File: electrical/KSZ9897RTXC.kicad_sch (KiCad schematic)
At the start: 1 part, among them U1 KSZ9897RTXC

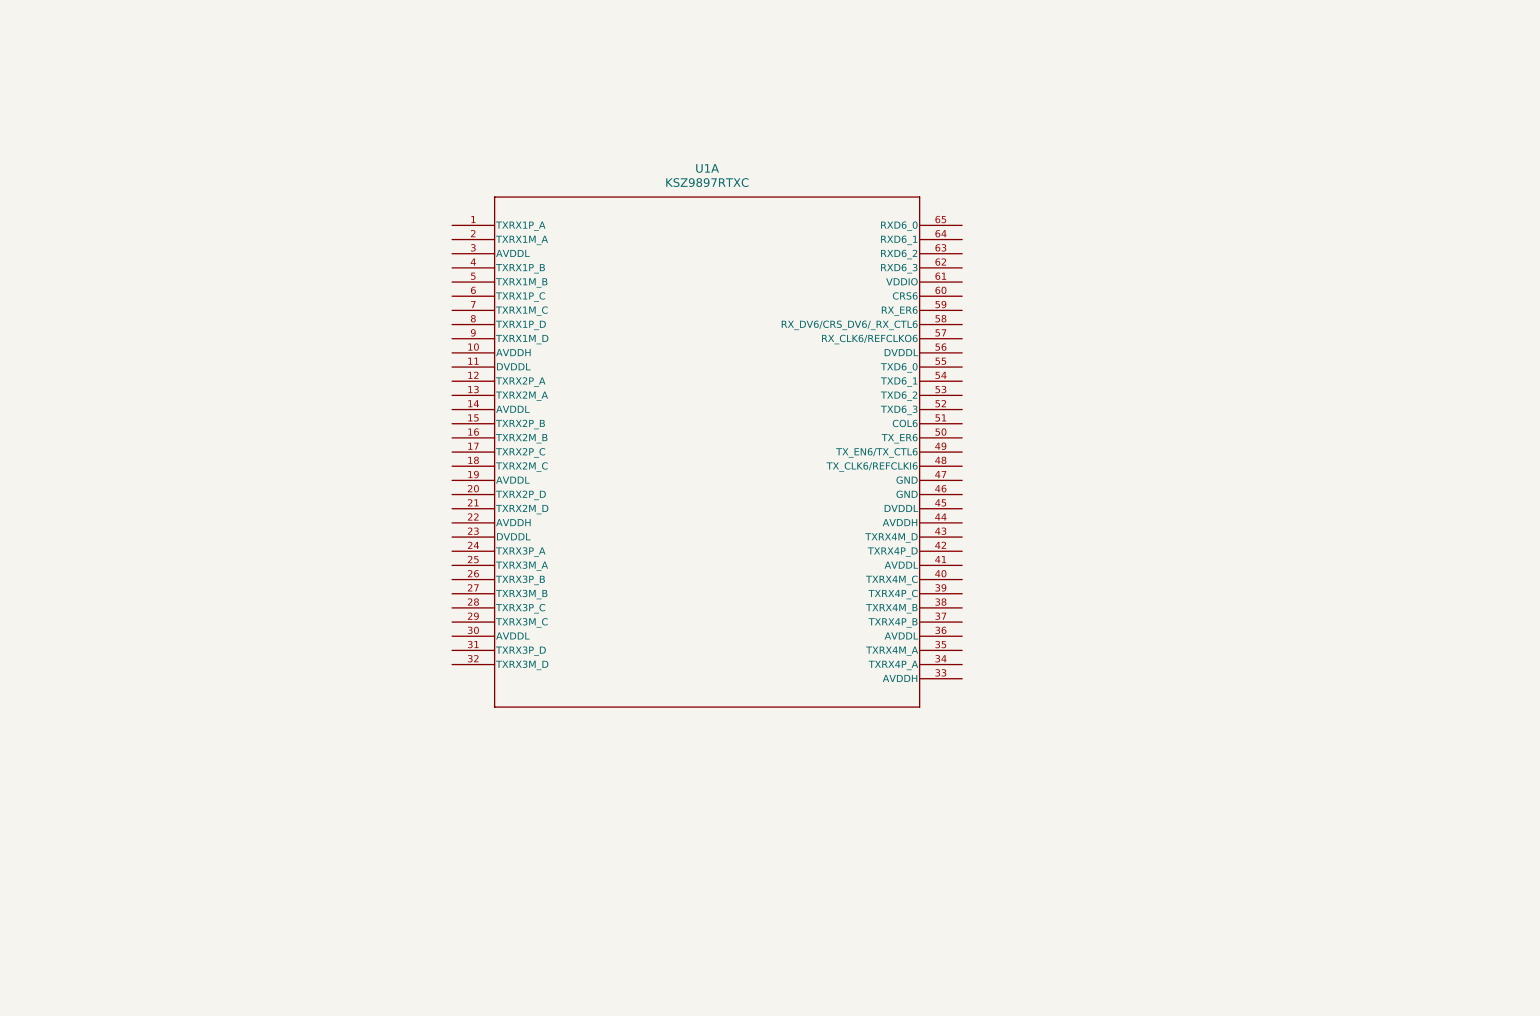
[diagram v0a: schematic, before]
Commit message: RJ-45 <-> KSZ9897R schematic connections
Also switched to a different RJ-45 port: Belfuse 0826-1G1T-23-F
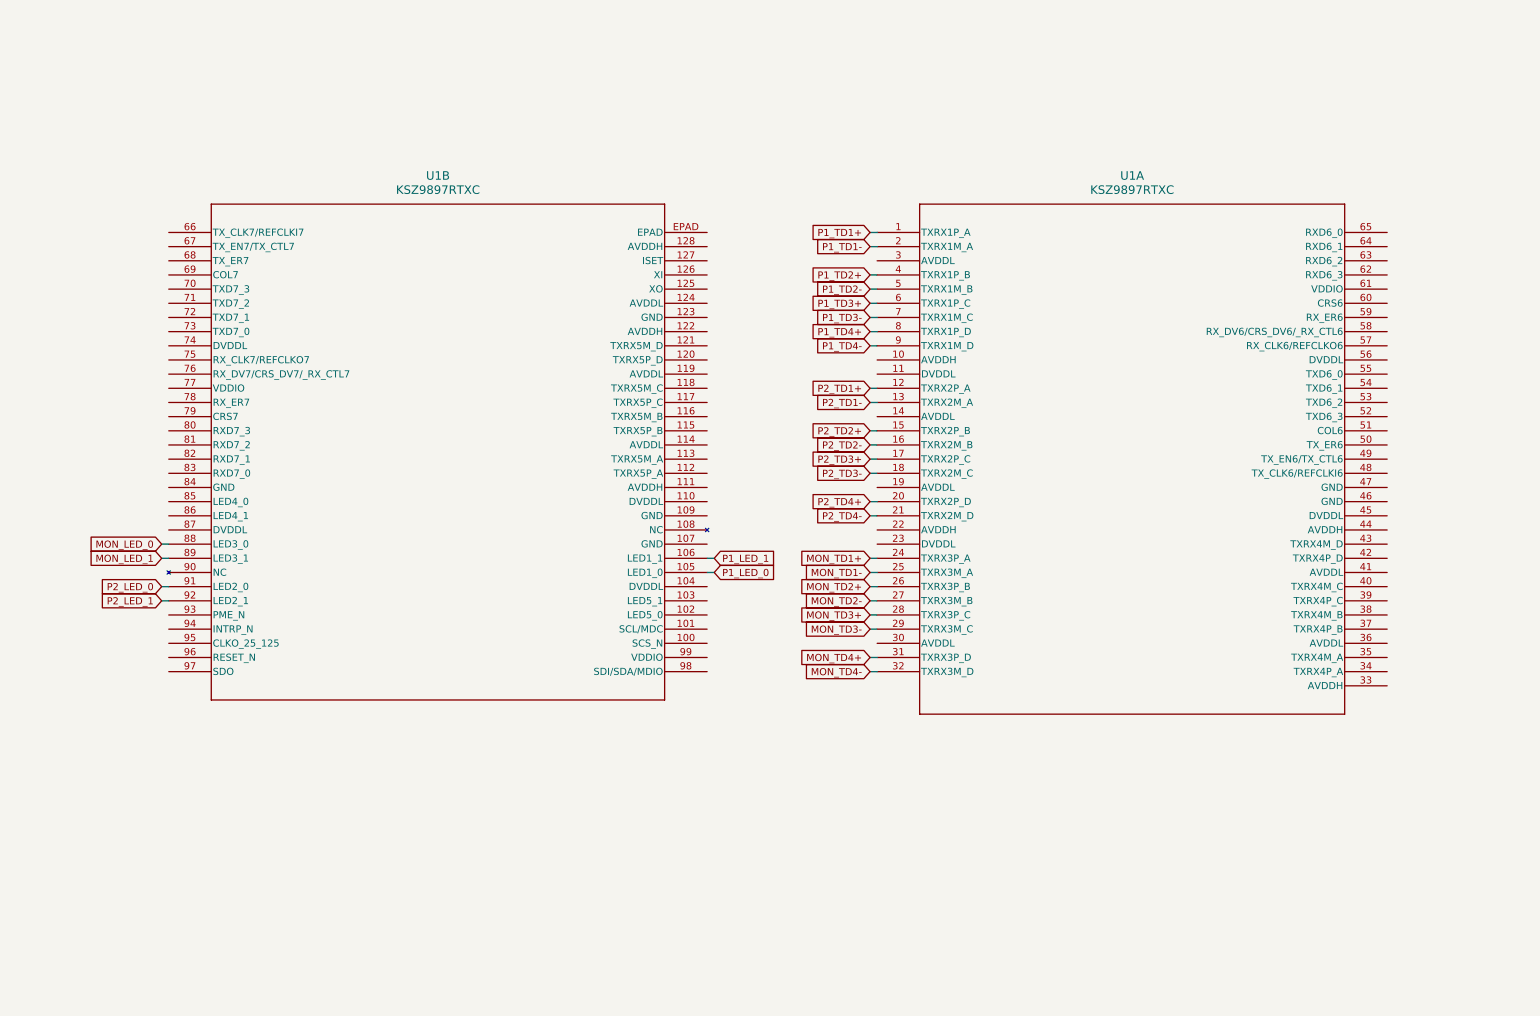
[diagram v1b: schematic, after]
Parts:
- added unit 2 of U1
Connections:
- net P1_TD1+: now reaches U1.1 (TXRX1P_A)
- net P2_TD1+: now reaches U1.12 (TXRX2P_A)
- net P2_TD1-: now reaches U1.13 (TXRX2M_A)
- net P2_TD2+: now reaches U1.15 (TXRX2P_B)
- net P2_TD2-: now reaches U1.16 (TXRX2M_B)
- net P2_TD3+: now reaches U1.17 (TXRX2P_C)
- net P2_TD3-: now reaches U1.18 (TXRX2M_C)
- net P1_TD1-: now reaches U1.2 (TXRX1M_A)
- net P2_TD4+: now reaches U1.20 (TXRX2P_D)
- net P2_TD4-: now reaches U1.21 (TXRX2M_D)
- net MON_TD1+: now reaches U1.24 (TXRX3P_A)
- net MON_TD1-: now reaches U1.25 (TXRX3M_A)
- net MON_TD2+: now reaches U1.26 (TXRX3P_B)
- net MON_TD2-: now reaches U1.27 (TXRX3M_B)
- net MON_TD3+: now reaches U1.28 (TXRX3P_C)
- net MON_TD3-: now reaches U1.29 (TXRX3M_C)
- net MON_TD4+: now reaches U1.31 (TXRX3P_D)
- net MON_TD4-: now reaches U1.32 (TXRX3M_D)
- net P1_TD2+: now reaches U1.4 (TXRX1P_B)
- net P1_TD2-: now reaches U1.5 (TXRX1M_B)
- net P1_TD3+: now reaches U1.6 (TXRX1P_C)
- net P1_TD3-: now reaches U1.7 (TXRX1M_C)
- net P1_TD4+: now reaches U1.8 (TXRX1P_D)
- net P1_TD4-: now reaches U1.9 (TXRX1M_D)
- new net MON_LED_0: U1.88 (LED3_0)
- new net MON_LED_1: U1.89 (LED3_1)
- new net P1_LED_0: U1.105 (LED1_0)
- new net P1_LED_1: U1.106 (LED1_1)
- new net P2_LED_0: U1.91 (LED2_0)
- new net P2_LED_1: U1.92 (LED2_1)
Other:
- moved on the sheet: U1A

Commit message: Add Pi LEDs + center tap connections
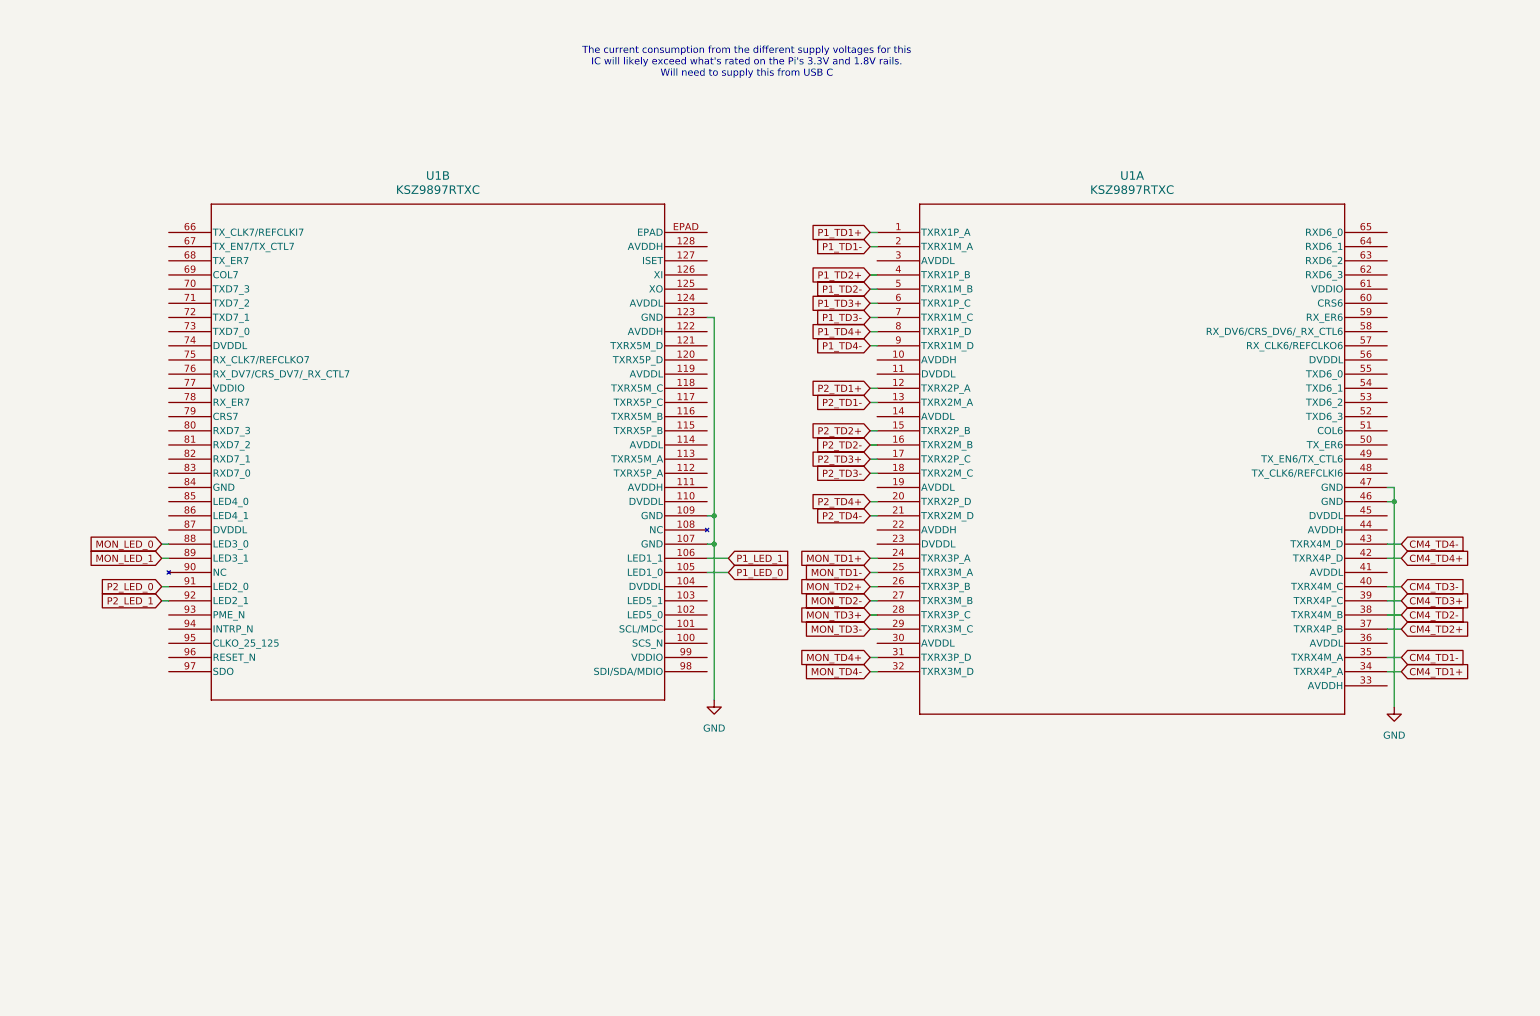
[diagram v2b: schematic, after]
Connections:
- net CM4_TD1+: now reaches U1.34 (TXRX4P_A)
- net CM4_TD1-: now reaches U1.35 (TXRX4M_A)
- net CM4_TD2+: now reaches U1.37 (TXRX4P_B)
- net CM4_TD2-: now reaches U1.38 (TXRX4M_B)
- net CM4_TD3+: now reaches U1.39 (TXRX4P_C)
- net CM4_TD3-: now reaches U1.40 (TXRX4M_C)
- net CM4_TD4+: now reaches U1.42 (TXRX4P_D)
- net CM4_TD4-: now reaches U1.43 (TXRX4M_D)
- net GND: now reaches U1.46 (GND)
- net GND: now also U1.107 (GND), U1.109 (GND), U1.123 (GND), U1.47 (GND)
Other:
- note added: "The current consumption from the different supply voltages for this IC will likely exceed what's rated on the Pi's 3.3V and 1.8V rails. Will need to supply this from USB C"

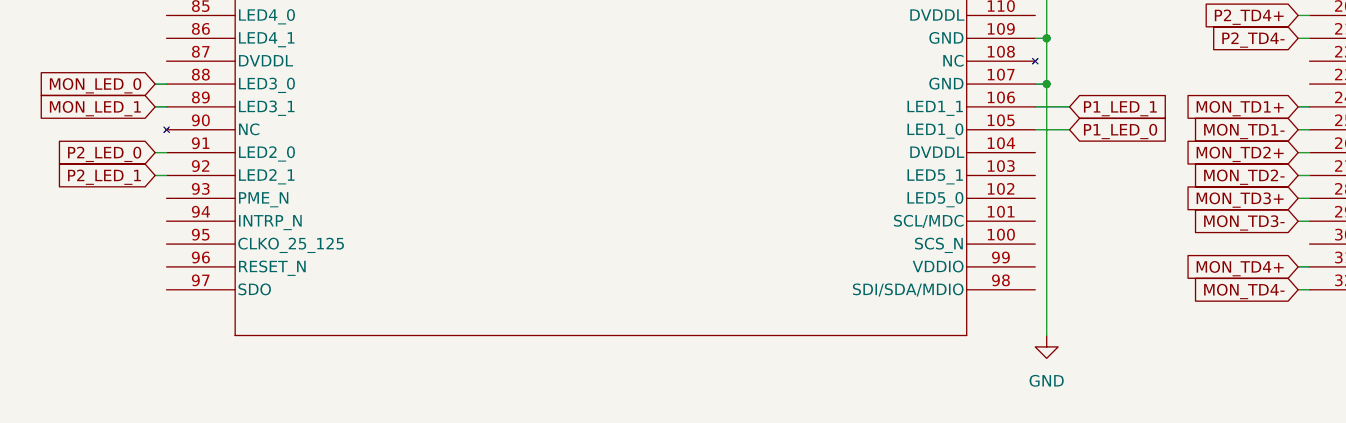
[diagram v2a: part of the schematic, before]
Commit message: Pi <-> Switch SPI interface
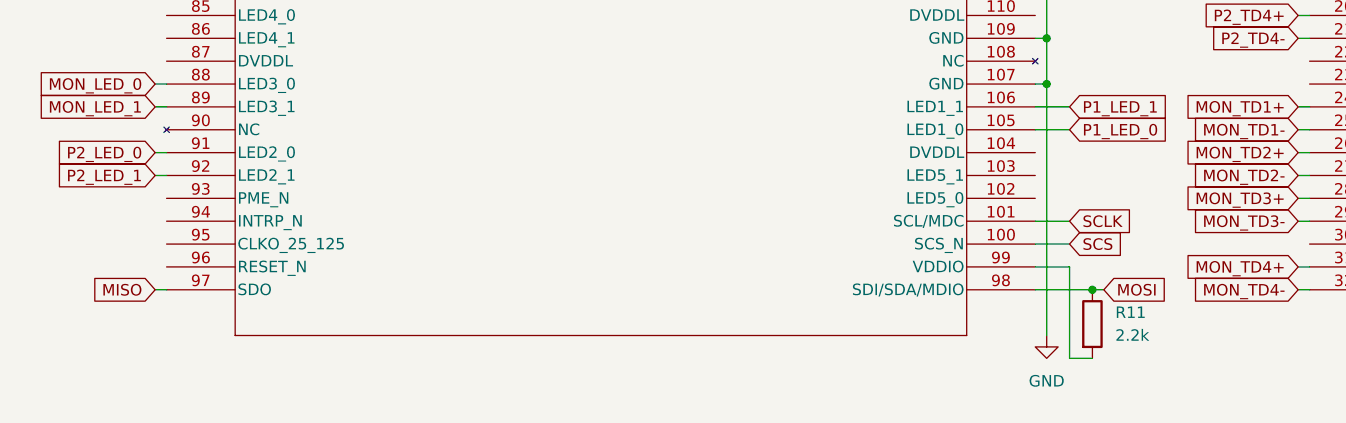
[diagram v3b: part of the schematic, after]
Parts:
- added R11: 2.2k, symbol Device:R
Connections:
- net SCS: now reaches U1.100 (SCS_N)
- net SCLK: now reaches U1.101 (SCL/MDC)
- net MISO: now reaches U1.97 (SDO)
- net MOSI: now reaches U1.98 (SDI/SDA/MDIO)
- net MOSI: now also R11.1
- net at U1.99 (VDDIO): now also R11.2
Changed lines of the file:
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@@
 		(color 0 0 0 0)
 	)
+	(junction
+		(at 143.51 133.35)
+		(diameter 0)
+		(color 0 0 0 0)
+	)
 	(wire
 		(pts
@@
 	(wire
 		(pts
+			(xy 140.97 130.81) (xy 137.16 130.81)
+		)
+		(stroke
+			(width 0)
+			(type default)
+		)
+	)
+	(wire
+		(pts
+			(xy 143.51 133.35) (xy 144.78 133.35)
+		)
+		(stroke
+			(width 0)
+			(type default)
+		)
+	)
+	(wire
+		(pts
+			(xy 137.16 128.27) (xy 140.97 128.27)
+		)
+		(stroke
+			(width 0)
+			(type default)
+		)
+	)
+	(wire
+		(pts
 			(xy 39.37 118.11) (xy 40.64 118.11)
 		)
@@
 	(wire
 		(pts
+			(xy 137.16 133.35) (xy 143.51 133.35)
+		)
+		(stroke
+			(width 0)
+			(type default)
+		)
+	)
+	(wire
+		(pts
 			(xy 39.37 110.49) (xy 40.64 110.49)
 		)
@@
 	(wire
 		(pts
+			(xy 143.51 140.97) (xy 140.97 140.97)
+		)
+		(stroke
+			(width 0)
+			(type default)
+		)
+	)
+	(wire
+		(pts
 			(xy 166.37 105.41) (xy 167.64 105.41)
 		)
@@
 	(wire
 		(pts
+			(xy 140.97 140.97) (xy 140.97 130.81)
+		)
+		(stroke
+			(width 0)
+			(type default)
+		)
+	)
+	(wire
+		(pts
 			(xy 39.37 113.03) (xy 40.64 113.03)
 		)
@@
 	(wire
 		(pts
+			(xy 39.37 133.35) (xy 40.64 133.35)
+		)
+		(stroke
+			(width 0)
+			(type default)
+		)
+	)
+	(wire
+		(pts
 			(xy 166.37 115.57) (xy 167.64 115.57)
 		)
@@
 		(pts
 			(xy 138.43 105.41) (xy 137.16 105.41)
+		)
+		(stroke
+			(width 0)
+			(type default)
+		)
+	)
+	(wire
+		(pts
+			(xy 137.16 125.73) (xy 140.97 125.73)
 		)
 		(stroke
@@
 		)
 	)
+	(global_label "MOSI"
+		(shape input)
+		(at 144.78 133.35 0)
+		(fields_autoplaced yes)
+		(effects
+			(font
+				(size 1.27 1.27)
+			)
+			(justify left)
+		)
+		(property "Intersheetrefs" "${INTERSHEET_REFS}"
+			(at 152.4565 133.35 0)
+			(effects
+				(font
+					(size 1.27 1.27)
+				)
+				(justify left)
+				(hide yes)
+			)
+		)
+	)
 	(global_label "P2_TD1-"
 		(shape input)
@@
 		)
 	)
+	(global_label "SCLK"
+		(shape input)
+		(at 140.97 125.73 0)
+		(fields_autoplaced yes)
+		(effects
+			(font
+				(size 1.27 1.27)
+			)
+			(justify left)
+		)
+		(property "Intersheetrefs" "${INTERSHEET_REFS}"
+			(at 148.8279 125.73 0)
+			(effects
+				(font
+					(size 1.27 1.27)
+				)
+				(justify left)
+				(hide yes)
+			)
+		)
+	)
 	(global_label "MON_TD3+"
 		(shape input)
@@
 		)
 	)
+	(global_label "SCS"
+		(shape input)
+		(at 140.97 128.27 0)
+		(fields_autoplaced yes)
+		(effects
+			(font
+				(size 1.27 1.27)
+			)
+			(justify left)
+		)
+		(property "Intersheetrefs" "${INTERSHEET_REFS}"
+			(at 147.7393 128.27 0)
+			(effects
+				(font
+					(size 1.27 1.27)
+				)
+				(justify left)
+				(hide yes)
+			)
+		)
+	)
 	(global_label "P2_TD4+"
 		(shape input)
@@
 		(property "Intersheetrefs" "${INTERSHEET_REFS}"
 			(at 153.1902 133.35 0)
+			(effects
+				(font
+					(size 1.27 1.27)
+				)
+				(justify right)
+				(hide yes)
+			)
+		)
+	)
+	(global_label "MISO"
+		(shape input)
+		(at 39.37 133.35 180)
+		(fields_autoplaced yes)
+		(effects
+			(font
+				(size 1.27 1.27)
+			)
+			(justify right)
+		)
+		(property "Intersheetrefs" "${INTERSHEET_REFS}"
+			(at 31.6935 133.35 0)
 			(effects
 				(font
@@
 					(unit 1)
 				)
+			)
+		)
+	)
+	(symbol
+		(lib_id "Device:R")
+		(at 143.51 137.16 0)
+		(unit 1)
+		(exclude_from_sim no)
+		(in_bom yes)
+		(on_board yes)
+		(dnp no)
+		(fields_autoplaced yes)
+		(property "Reference" "R11"
+			(at 146.05 135.8899 0)
+			(effects
+				(font
+					(size 1.27 1.27)
+				)
+				(justify left)
+			)
+		)
+		(property "Value" "2.2k"
+			(at 146.05 138.4299 0)
+			(effects
+				(font
+					(size 1.27 1.27)
+				)
+				(justify left)
+			)
+		)
+		(property "Footprint" ""
+			(at 141.732 137.16 90)
+			(effects
+				(font
+					(size 1.27 1.27)
+				)
+				(hide yes)
+			)
+		)
+		(property "Datasheet" "~"
+			(at 143.51 137.16 0)
+			(effects
+				(font
+					(size 1.27 1.27)
+				)
+				(hide yes)
+			)
+		)
+		(property "Description" "Resistor"
+			(at 143.51 137.16 0)
+			(effects
+				(font
+					(size 1.27 1.27)
+				)
+				(hide yes)
+			)
+		)
+		(pin "1"
+		)
+		(pin "2"
+		)
+		(instances
+			(project ""
+				(path "/87b93ef3-3469-436c-9ae8-16e6c9607244/a750164c-9325-431d-9312-5cb40f11da35"
+					(reference "R11")
+					(unit 1)
+				)
